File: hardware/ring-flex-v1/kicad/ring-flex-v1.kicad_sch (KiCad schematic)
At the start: 28 parts, among them J1 charge pad +, J2 charge pad -, M1 NFP-C1020 10x2.0mm ERM, Q1A FS8205A Q1 (discharge), Q1B FS8205A Q2 (charge), Q2 AO3400A, U1 MDBT50Q-1MV2, U2 MCP73831-2, U3 TPS7A0230PDBVR 3.0V, U4 DW01A

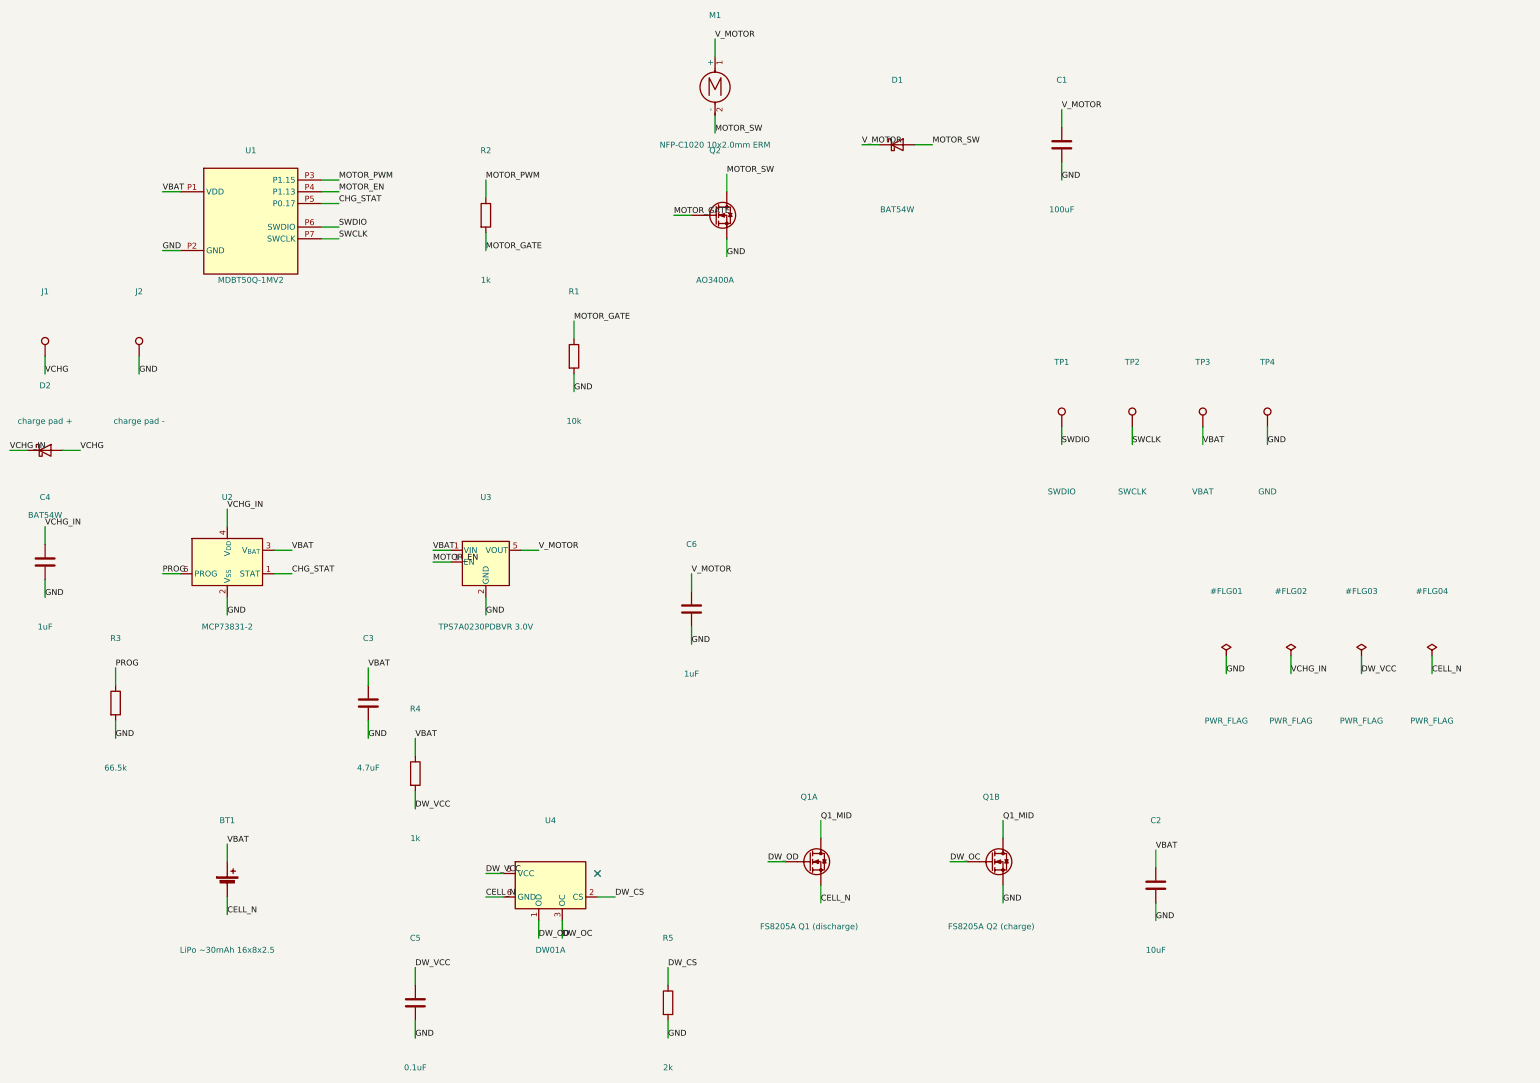
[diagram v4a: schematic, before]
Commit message: Hardware: charge pads and an unpopulated USB-C
Charge contacts are now real 2 x 2 mm pads rather than 1 mm test points,
in a footprint that deliberately omits the paste layer: these are contact
surfaces for pogo pins, not solder joints. Specify ENIG so they do not
corrode against a spring contact.

USB-C added as pads only, DO NOT POPULATE, per the decision to charge
through the dock and flash over SWD. It is insurance: if BLE DFU fights
back during bring-up, populating this restores the UF2/serial path the XIAO
has today. It is a 16P footprint because its pads are a superset of the
power-only symbol's pins; the data pads simply go unused.

R6 and R7, 5.1 k on CC1 and CC2, are not optional -- without them a USB-C
source sees no sink and supplies nothing. That is the usual way a first
USB-C design fails.

VBUS joins the same VCHG net as the pogo pads, so D2's reverse-polarity
guard protects both paths.

Verified in the netlist: VCHG carries D2.2, J1.1 and all four J3 VBUS pins;
USB_CC1 and USB_CC2 each reach their pulldown. ERC back to the single
cosmetic lib_symbol_mismatch. U1 remains the only part without a footprint.

Co-Authored-By: Claude Opus 5 <noreply@anthropic.com>
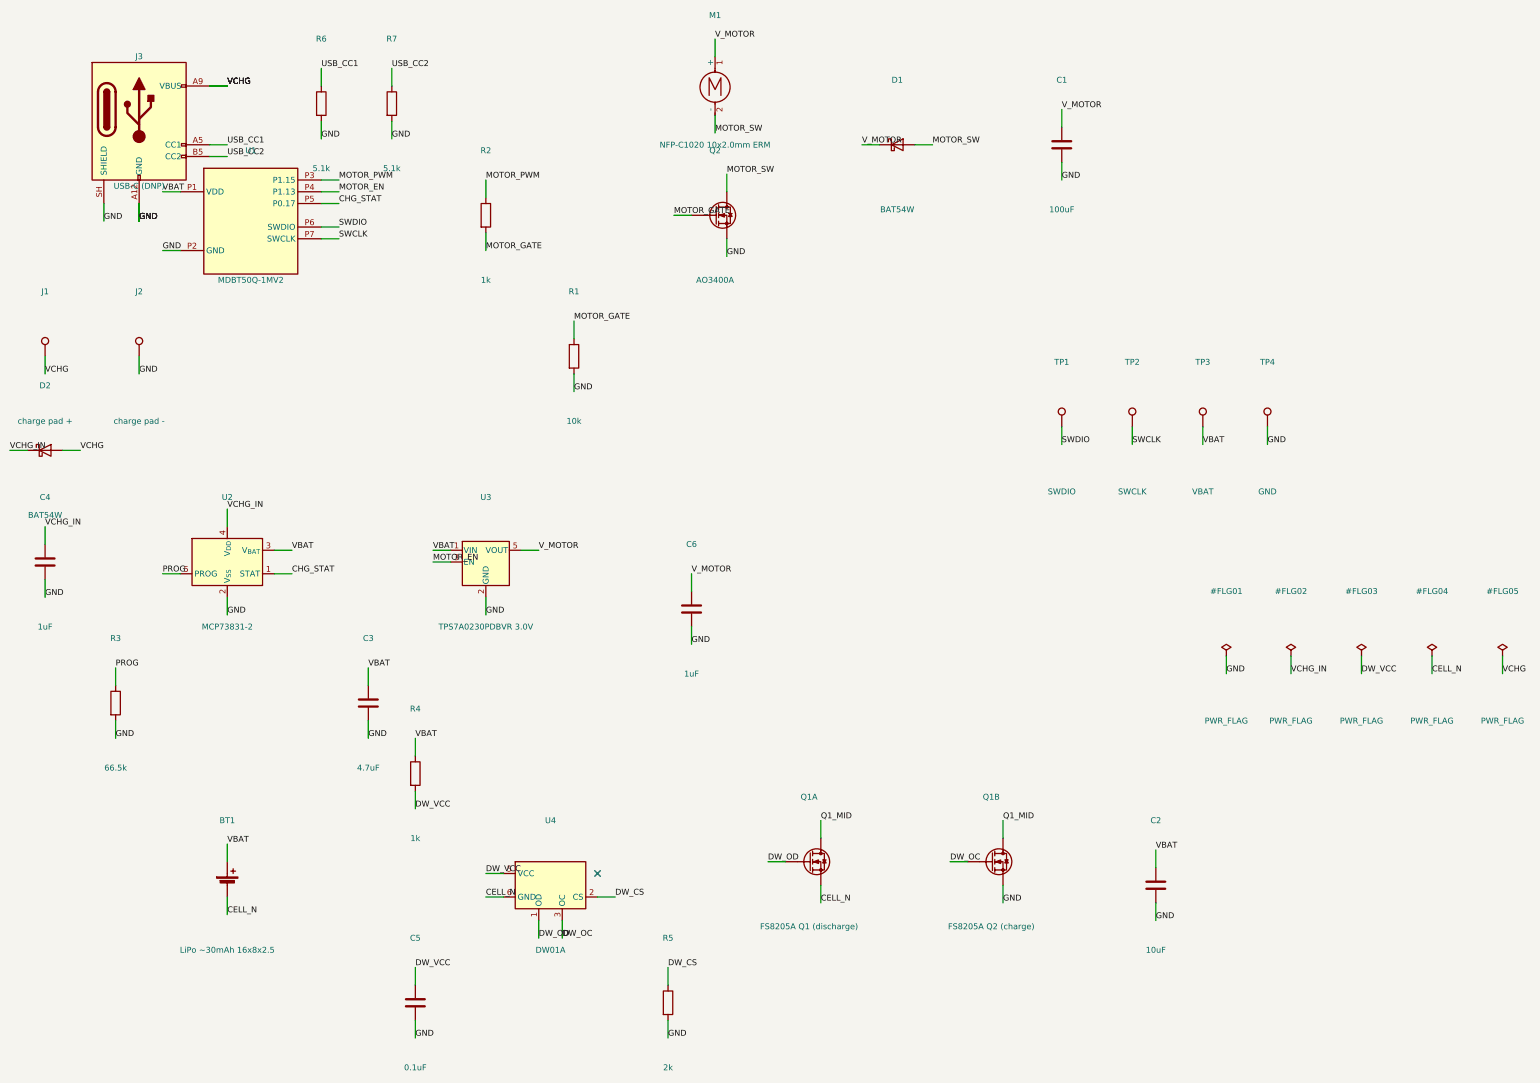
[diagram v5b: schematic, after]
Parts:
- added J3: USB-C (DNP), Connector_USB:USB_C_Receptacle_HCTL_HC-TYPE-C-16P-01A, symbol Connector:USB_C_Receptacle_PowerOnly_24P
- added R6, R7: 5.1k, Resistor_SMD:R_0402_1005Metric, symbol Device:R
- J1, J2: footprint TestPoint:TestPoint_Pad_D1.0mm -> ring-flex-v1:ChargePad_2x2mm
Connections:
- net GND: now also J3.A1 (GND), J3.A12 (GND), J3.B1 (GND), J3.B12 (GND), J3.SH (SHIELD), R6.2, R7.2
- net VCHG: now also J3.A4 (VBUS), J3.A9 (VBUS), J3.B4 (VBUS), J3.B9 (VBUS)
- new net USB_CC1: J3.A5 (CC1), R6.1
- new net USB_CC2: J3.B5 (CC2), R7.1

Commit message: Hardware: module footprint adopted and verified; every part now has one
U1 was the last component without a footprint. Rather than reconstruct 61
pad positions from a drawing, I took the public one from
github.com/famichu/kicad_libs_MDBT50, upgraded it to the current format, and
checked it against Raytac's approval sheet:

  pad count       61            vs 61
  pad size        0.6 x 0.4 mm  vs all 0.6 x 0.4 (36 landscape, 25 rotated)
  numbering       1-61          vs contiguous 1-61
  pad field       ~11.7 mm tall vs 10.90 centre-to-centre, ~11.5 outer

Everything checkable agrees. The 0.2 mm on field height is within how a
dimension is read off a drawing.

What I did NOT verify, and cannot from geometry alone: that pin 1 is where
this footprint puts it. That needs the datasheet's pin table against
Raytac's own footprint, and it is recorded as a pre-fab check in both the
README and the BOM.

All 31 components now carry a footprint. ERC is at one cosmetic
lib_symbol_mismatch.

Co-Authored-By: Claude Opus 5 <noreply@anthropic.com>
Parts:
- U1: footprint (none) -> ring-flex-v1:MDBT50Q-1MV2

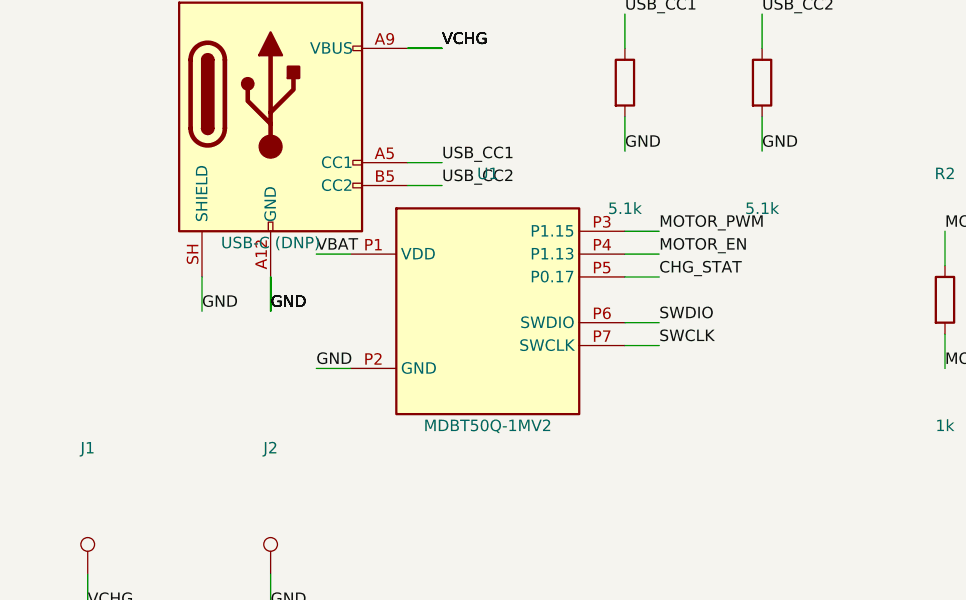
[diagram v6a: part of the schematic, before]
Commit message: Hardware: real module pins, and the supply moves to VDDH
Two findings from the approval sheet, one of them a design error.

PIN NUMBERS ARE REAL NOW. Section 2.5's table gives them: GND on 1, 2, 15,
33 and 55; P1.13 = 6; P1.15 = 8; P0.17 = 41; VDD = 28; VDDH = 30;
SWDIO = 51; SWDCLK = 53. The P1-P7 placeholders are gone, and with them the
largest remaining unknown in the schematic.

THE SUPPLY WAS ON THE WRONG PIN. I had the cell feeding VDD. Section 8 of
the datasheet says to supply VDDH when the input can reach 3.6 V or more,
and a full LiPo is 4.2 V against a 3.6 V maximum on VDD. The cell now feeds
pin 30 (VDDH); pin 28 (VDD) is REG0's output and gets C7, a decoupling cap,
nothing else.

That brings a firmware obligation with it: REGOUT0 defaults to 1.8 V on a
fresh part and every GPIO level follows it. At 1.8 V the motor gate would
sit around the AO3400's threshold and the drive would be marginal at best.
REGOUT0 has to be set to 3.0 or 3.3 V in UICR. The Adafruit bootloader
normally handles it; it still needs checking rather than assuming.

REG0 runs in LDO mode for v1, so no inductor. DC/DC would need L4 = 10 uH
0603 at IDC >= 80 mA and only pays off during radio bursts.

Footprint geometry is now verified exactly rather than approximately: the
dimensioned layout in section 2.5 gives pad X 0.45-10.05 and Y 0.6-11.5, and
the adopted footprint spans precisely those ranges.

All 32 components have footprints. ERC: one cosmetic lib_symbol_mismatch.
Firmware tests 450/0.

Co-Authored-By: Claude Opus 5 <noreply@anthropic.com>
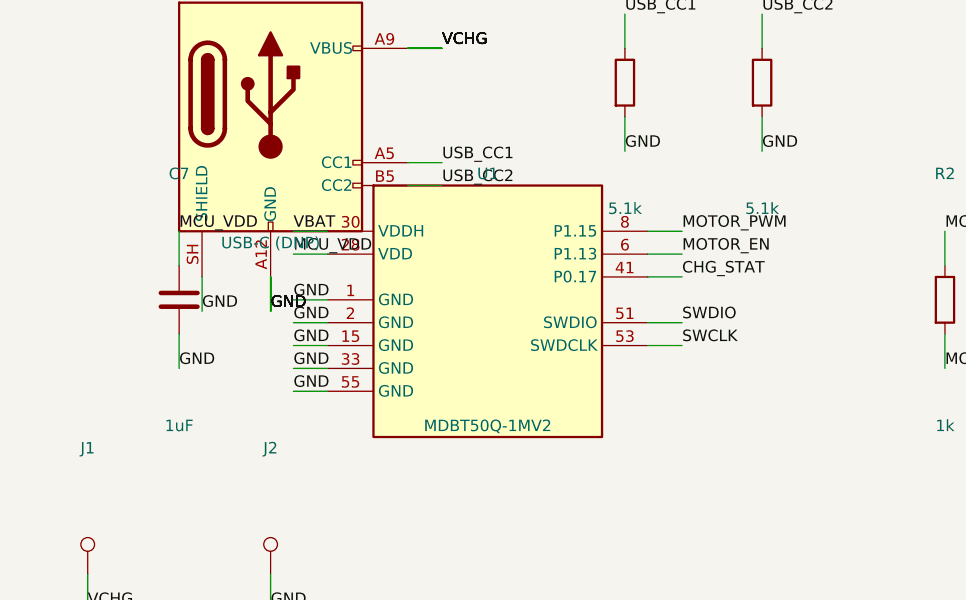
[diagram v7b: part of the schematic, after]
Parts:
- added C7: 1uF, Capacitor_SMD:C_0402_1005Metric, symbol Device:C
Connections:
- net CHG_STAT: now also U1.41 (P0.17); no longer U1.P5 (P0.17)
- net GND: now also U1.1 (GND), U1.15 (GND), U1.2 (GND), U1.33 (GND), U1.55 (GND), C7.2; no longer U1.P2 (GND)
- net MOTOR_EN: now also U1.6 (P1.13); no longer U1.P4 (P1.13)
- net MOTOR_PWM: now also U1.8 (P1.15); no longer U1.P3 (P1.15)
- net SWCLK: now also U1.53 (SWDCLK); no longer U1.P7 (SWCLK)
- net SWDIO: now also U1.51 (SWDIO); no longer U1.P6 (SWDIO)
- net VBAT: now also U1.30 (VDDH); no longer U1.P1 (VDD)
- new net MCU_VDD: C7.1, U1.28 (VDD)

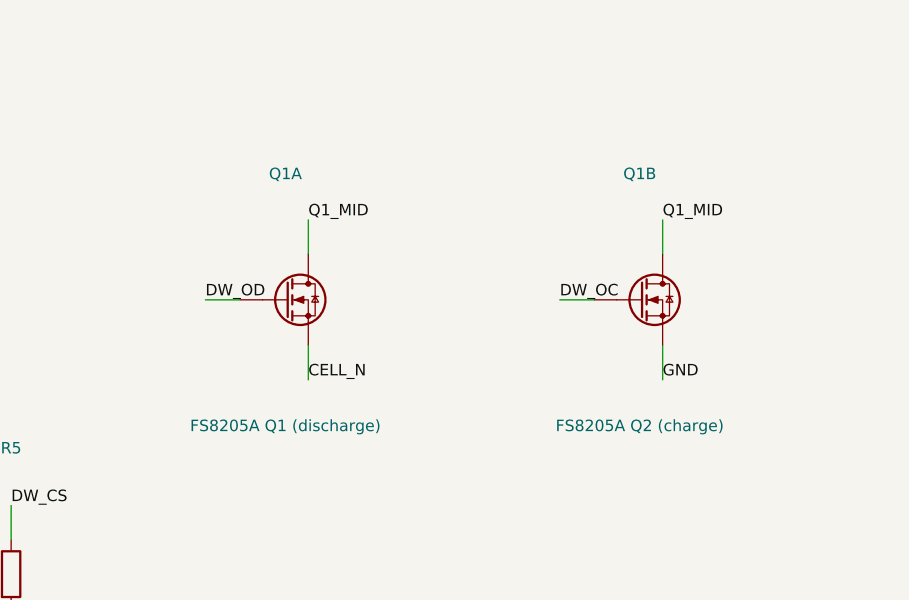
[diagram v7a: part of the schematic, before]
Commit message: Hardware: FS8205A is one part, drawn as one symbol
The schematic had the protection FETs as two Q_NMOS symbols, Q1A and Q1B.
They are one physical device, so the board would have carried two SOT-23-6
footprints for a single FS8205A. Caught by cross-checking the BOM against
the netlist -- the BOM said Q1, the netlist said Q1A and Q1B.

Replaced with a proper 6-pin FS8205A symbol in the project library. The
pinout is read off the datasheet's marking diagram, where the pin-1 dot sits
beside S1:

  1 = S1   2 = D1/D2   3 = S2   4 = G2   5 = D1/D2   6 = G1

Wired as: S1 to the cell negative, S2 to pack negative, G1 to the DW01A's
discharge control and G2 to its charge control, with pins 2 and 5 forming
the shared drain.

Verified: CELL_N carries BT1.2, Q1.1 and U4.6; Q1_MID carries Q1.2 and Q1.5;
the gates reach their respective DW01A outputs. BOM and netlist reference
lists now match exactly.

Co-Authored-By: Claude Opus 5 <noreply@anthropic.com>
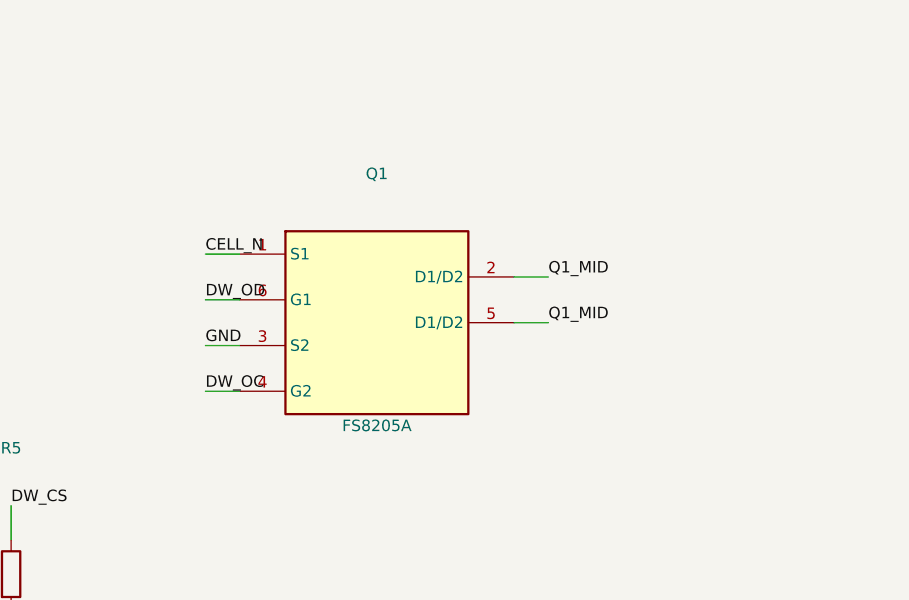
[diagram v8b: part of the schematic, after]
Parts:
- removed Q1A: FS8205A Q1 (discharge), Package_TO_SOT_SMD:SOT-23-6, symbol Device:Q_NMOS
- removed Q1B: FS8205A Q2 (charge), Package_TO_SOT_SMD:SOT-23-6, symbol Device:Q_NMOS
- added Q1: FS8205A, Package_TO_SOT_SMD:SOT-23-6, symbol ring-flex-v1:FS8205A
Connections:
- net CELL_N: now also Q1.1 (S1)
- net DW_OC: now also Q1.4 (G2)
- net DW_OD: now also Q1.6 (G1)
- net GND: now also Q1.3 (S2)
- net Q1_MID: now also Q1.2 (D1/D2), Q1.5 (D1/D2)
